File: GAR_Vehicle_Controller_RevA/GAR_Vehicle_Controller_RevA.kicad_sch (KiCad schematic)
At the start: 0 parts

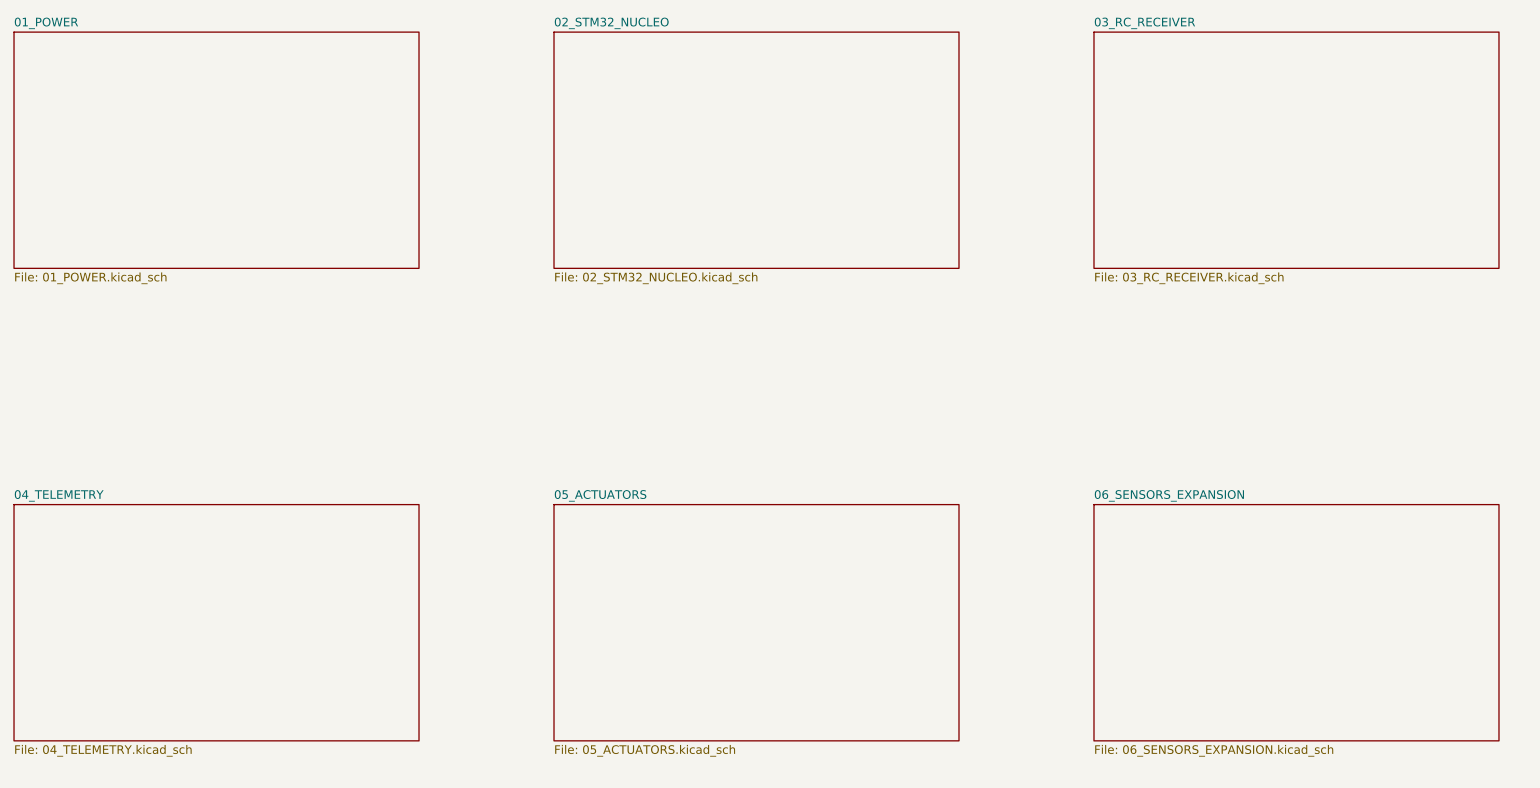
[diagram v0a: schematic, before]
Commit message: Draw first draft of the RC receiver sheet
03_RC_RECEIVER now has the J1 header, 0R series links, an unfitted
2N7002 inverter with a 0R bypass, supply bypass caps, and four test
points, ending in the RC_UART_RX / RC_UART_TX hierarchical labels.
The top sheet gains matching sheet pins and its sheet symbols are moved
onto the 2.54 mm grid. ERC reports four expected items until the other
sheets exist.
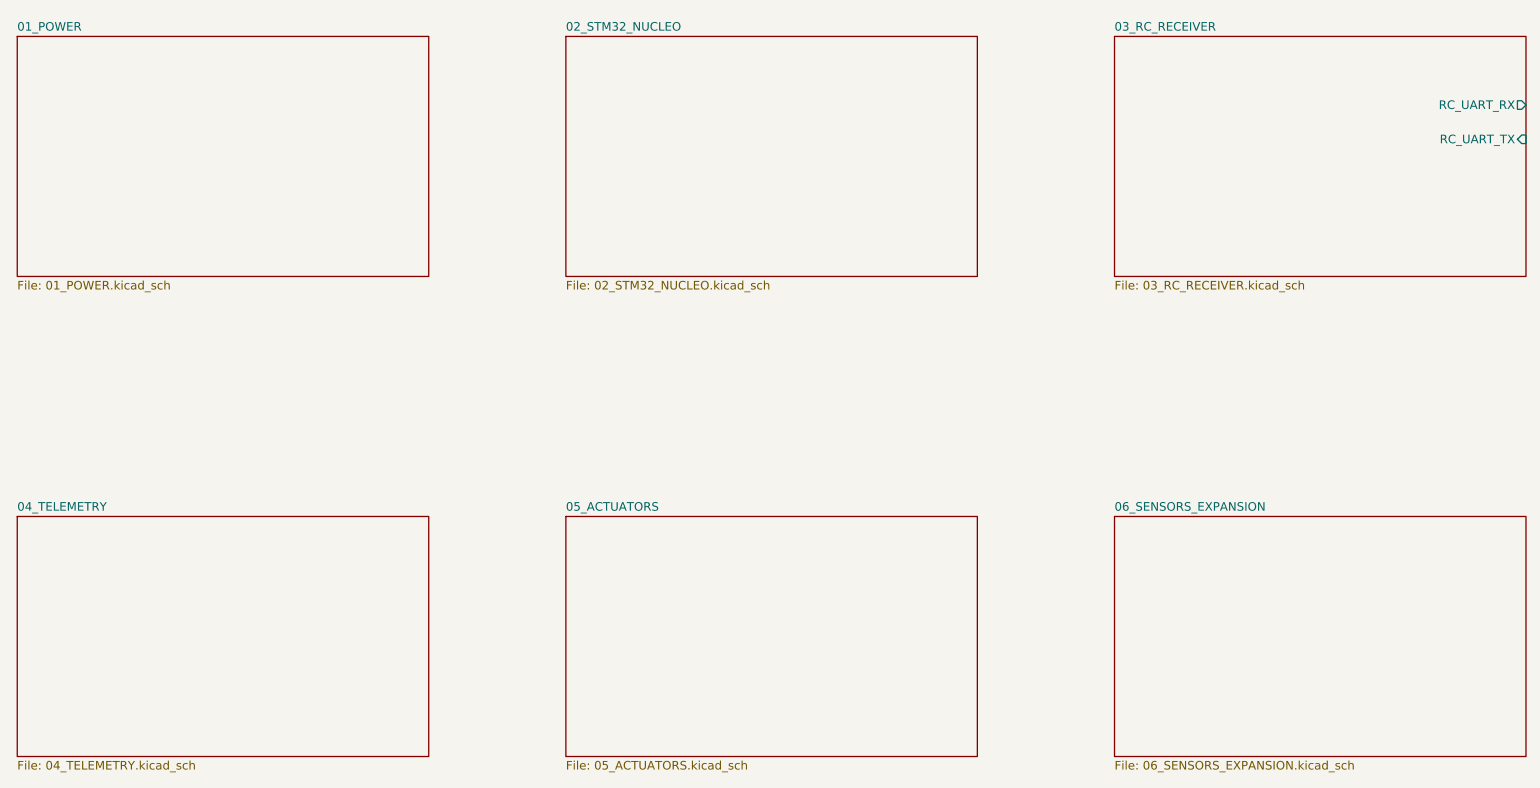
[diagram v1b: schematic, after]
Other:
- sheet 03_RC_RECEIVER ports: added RC_UART_RX, RC_UART_TX; removed none
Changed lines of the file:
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@@
 	)
 	(sheet
-		(at 190 110)
-		(size 60 35)
+		(at 193.04 111.76)
+		(size 60.96 35.56)
 		(exclude_from_sim no)
 		(in_bom yes)
@@
 		)
 		(property "Sheetname" "06_SENSORS_EXPANSION"
-			(at 190 109.3 0)
+			(at 193.04 111.06 0)
 			(show_name no)
 			(do_not_autoplace no)
@@
 		)
 		(property "Sheetfile" "06_SENSORS_EXPANSION.kicad_sch"
-			(at 190 145.6 0)
+			(at 193.04 147.92 0)
 			(show_name no)
 			(do_not_autoplace no)
@@
 	)
 	(sheet
-		(at 30 110)
-		(size 60 35)
+		(at 30.48 111.76)
+		(size 60.96 35.56)
 		(exclude_from_sim no)
 		(in_bom yes)
@@
 		)
 		(property "Sheetname" "04_TELEMETRY"
-			(at 30 109.3 0)
+			(at 30.48 111.06 0)
 			(show_name no)
 			(do_not_autoplace no)
@@
 		)
 		(property "Sheetfile" "04_TELEMETRY.kicad_sch"
-			(at 30 145.6 0)
+			(at 30.48 147.92 0)
 			(show_name no)
 			(do_not_autoplace no)
@@
 	)
 	(sheet
-		(at 30 40)
-		(size 60 35)
+		(at 30.48 40.64)
+		(size 60.96 35.56)
 		(exclude_from_sim no)
 		(in_bom yes)
@@
 		)
 		(property "Sheetname" "01_POWER"
-			(at 30 39.3 0)
+			(at 30.48 39.94 0)
 			(show_name no)
 			(do_not_autoplace no)
@@
 		)
 		(property "Sheetfile" "01_POWER.kicad_sch"
-			(at 30 75.6 0)
+			(at 30.48 76.8 0)
 			(show_name no)
 			(do_not_autoplace no)
@@
 	)
 	(sheet
-		(at 190 40)
-		(size 60 35)
+		(at 193.04 40.64)
+		(size 60.96 35.56)
 		(exclude_from_sim no)
 		(in_bom yes)
@@
 		)
 		(property "Sheetname" "03_RC_RECEIVER"
-			(at 190 39.3 0)
+			(at 193.04 39.94 0)
 			(show_name no)
 			(do_not_autoplace no)
@@
 		)
 		(property "Sheetfile" "03_RC_RECEIVER.kicad_sch"
-			(at 190 75.6 0)
-			(show_name no)
-			(do_not_autoplace no)
-			(effects
-				(font
-					(size 1.27 1.27)
-				)
-				(justify left top)
+			(at 193.04 76.8 0)
+			(show_name no)
+			(do_not_autoplace no)
+			(effects
+				(font
+					(size 1.27 1.27)
+				)
+				(justify left top)
+			)
+		)
+		(pin "RC_UART_RX" output
+			(at 254 50.8 0)
+			(effects
+				(font
+					(size 1.27 1.27)
+				)
+				(justify right)
+			)
+		)
+		(pin "RC_UART_TX" input
+			(at 254 55.88 0)
+			(effects
+				(font
+					(size 1.27 1.27)
+				)
+				(justify right)
 			)
 		)
@@
 	)
 	(sheet
-		(at 110 40)
-		(size 60 35)
+		(at 111.76 40.64)
+		(size 60.96 35.56)
 		(exclude_from_sim no)
 		(in_bom yes)
@@
 		)
 		(property "Sheetname" "02_STM32_NUCLEO"
-			(at 110 39.3 0)
+			(at 111.76 39.94 0)
 			(show_name no)
 			(do_not_autoplace no)
@@
 		)
 		(property "Sheetfile" "02_STM32_NUCLEO.kicad_sch"
-			(at 110 75.6 0)
+			(at 111.76 76.8 0)
 			(show_name no)
 			(do_not_autoplace no)
@@
 	)
 	(sheet
-		(at 110 110)
-		(size 60 35)
+		(at 111.76 111.76)
+		(size 60.96 35.56)
 		(exclude_from_sim no)
 		(in_bom yes)
@@
 		)
 		(property "Sheetname" "05_ACTUATORS"
-			(at 110 109.3 0)
+			(at 111.76 111.06 0)
 			(show_name no)
 			(do_not_autoplace no)
@@
 		)
 		(property "Sheetfile" "05_ACTUATORS.kicad_sch"
-			(at 110 145.6 0)
-			(show_name no)
-			(do_not_autoplace no)
+			(at 111.76 147.92 0)
+			(show_name no)
+			(do_not_autoplace no)
